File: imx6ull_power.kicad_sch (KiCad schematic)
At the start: 20 parts, among them U1 MX6UL-VM

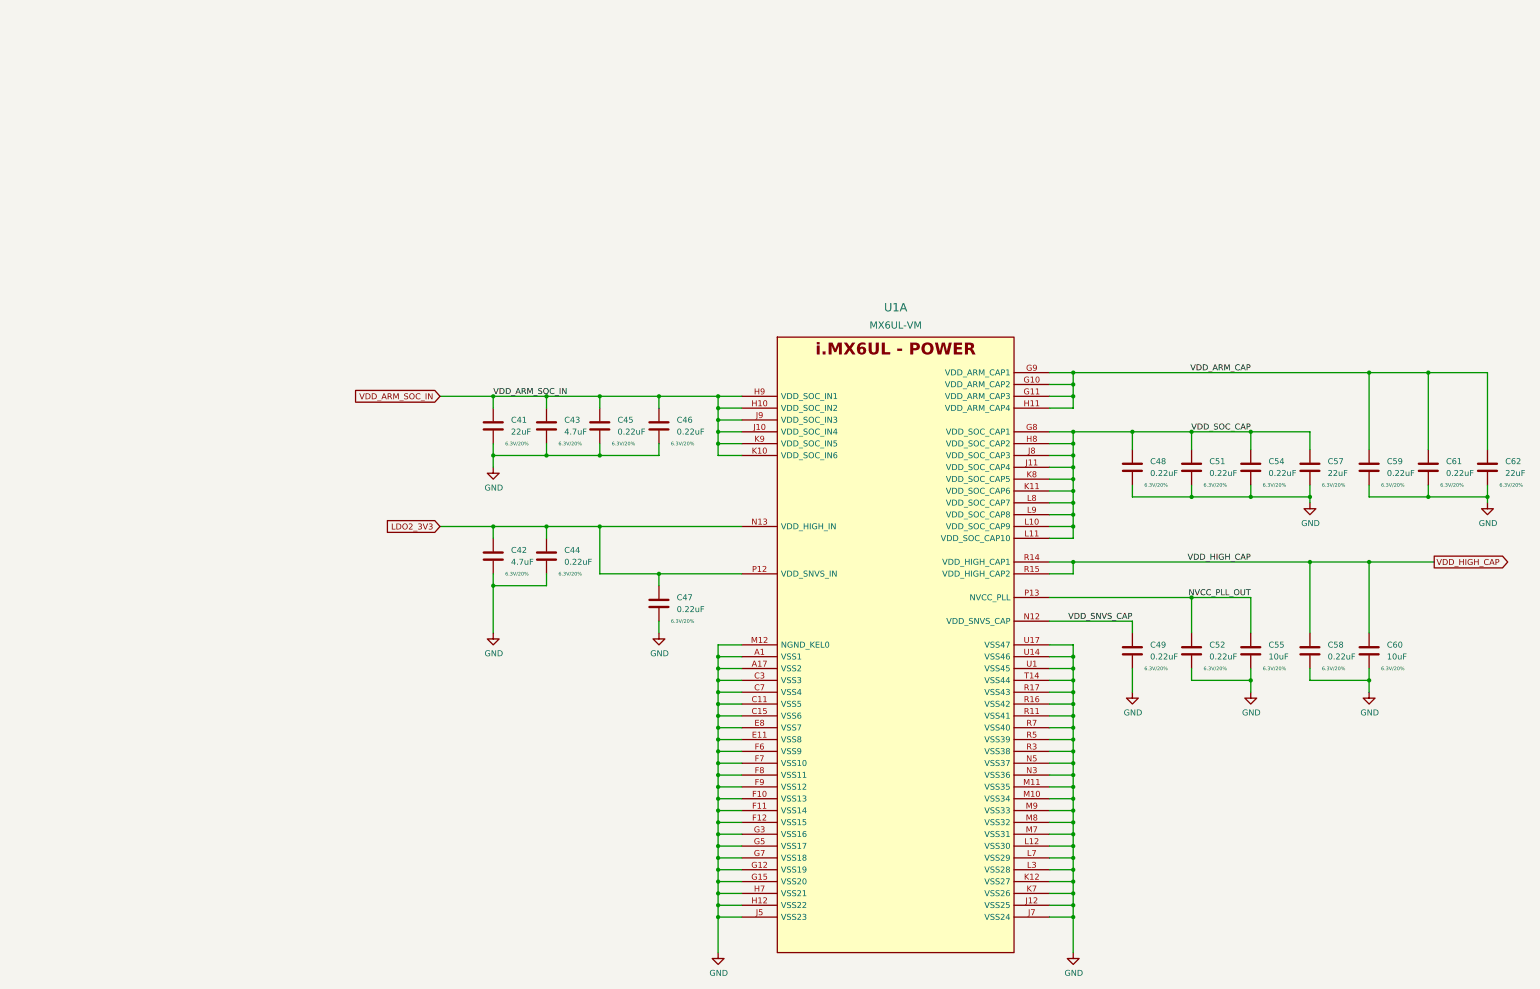
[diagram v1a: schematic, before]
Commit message: start moving to hierarchal labels, add emmc
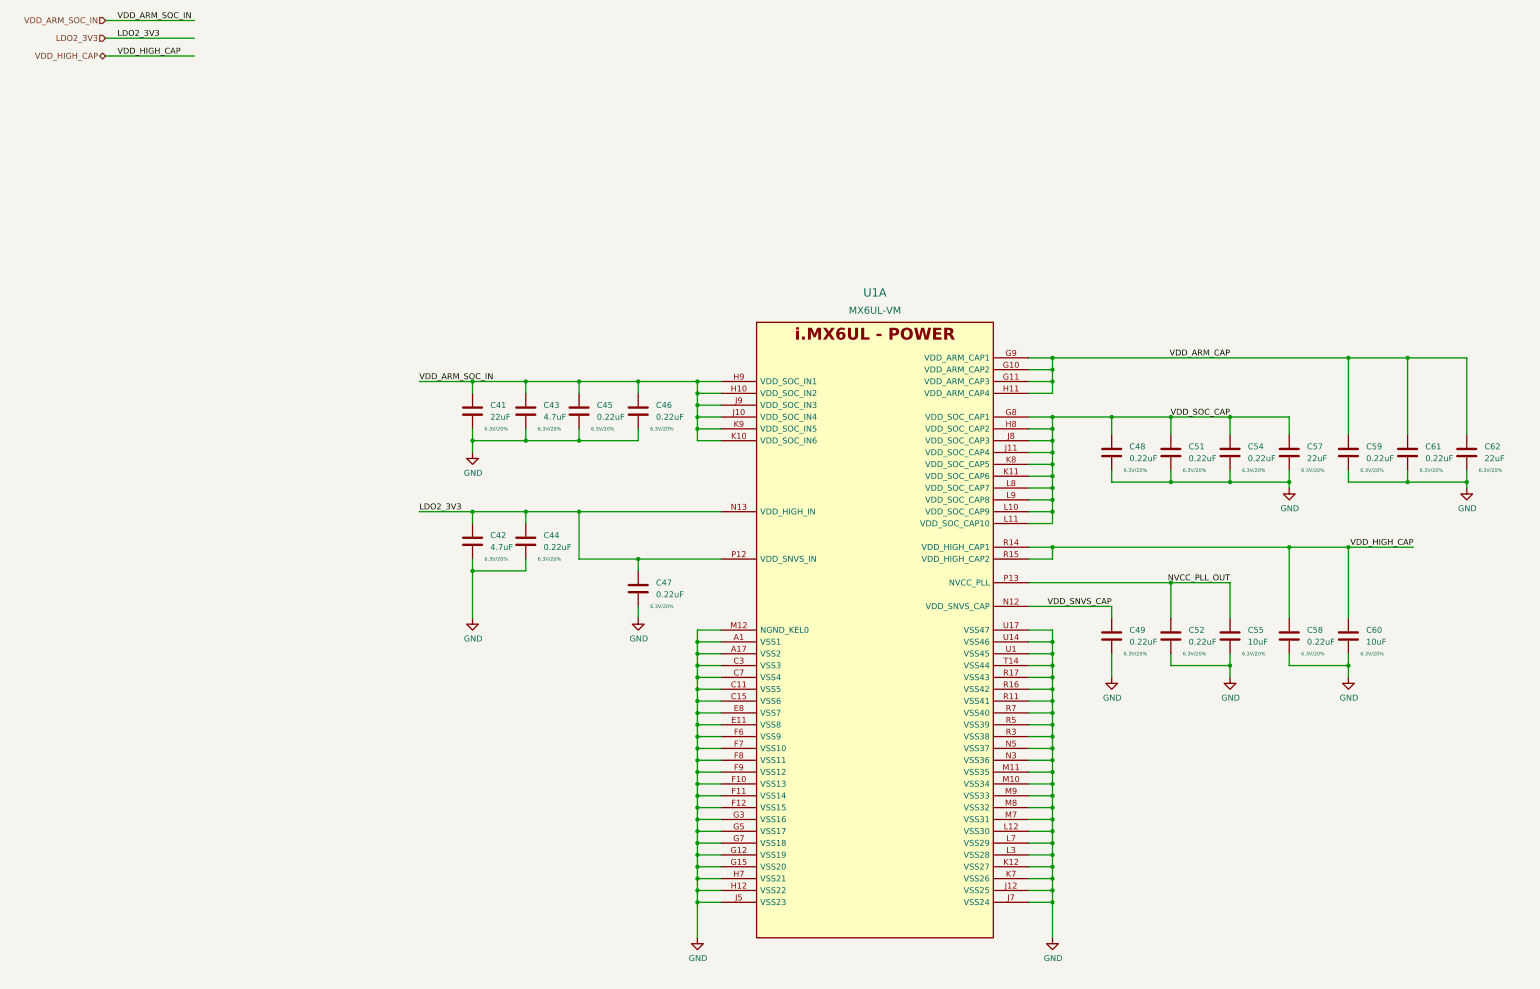
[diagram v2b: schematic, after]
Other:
- moved on the sheet: C41, C42, C43, C44, C45, C46, C47, C48, C49, C51, C52, C54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

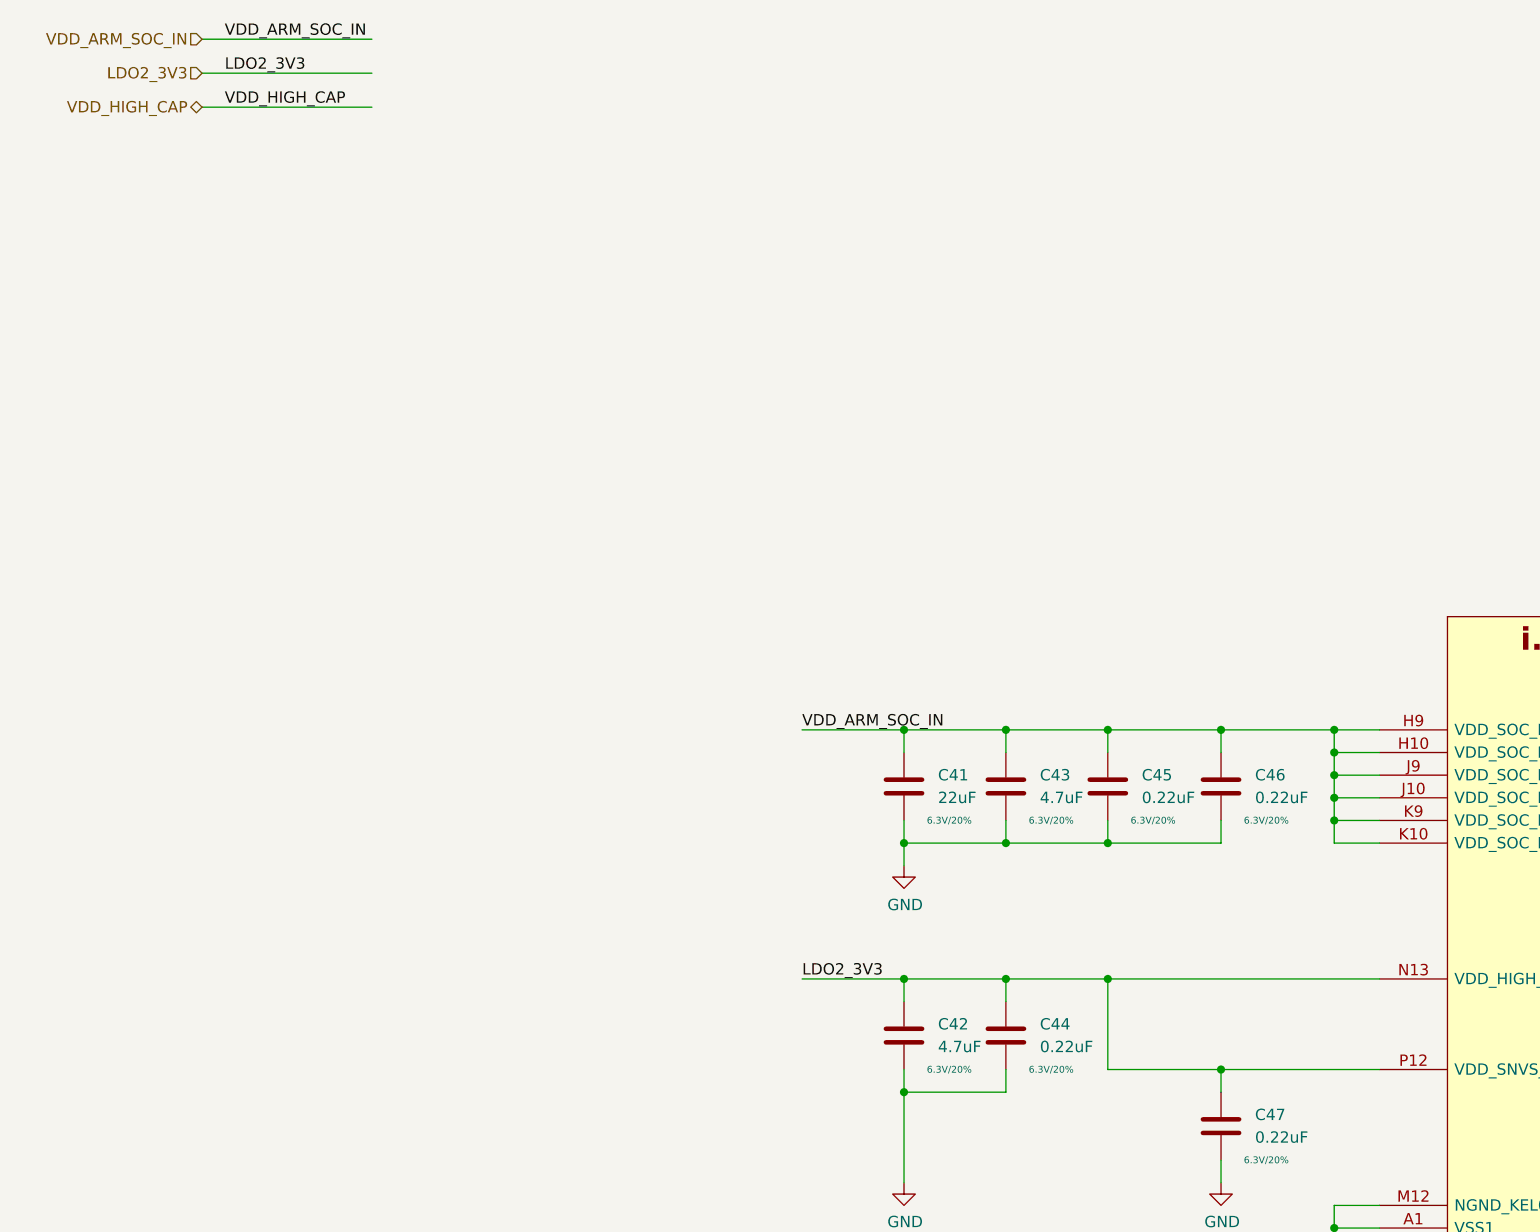
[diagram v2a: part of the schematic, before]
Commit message: move to hierarchal labels, work on power tree, add basic pcb layout
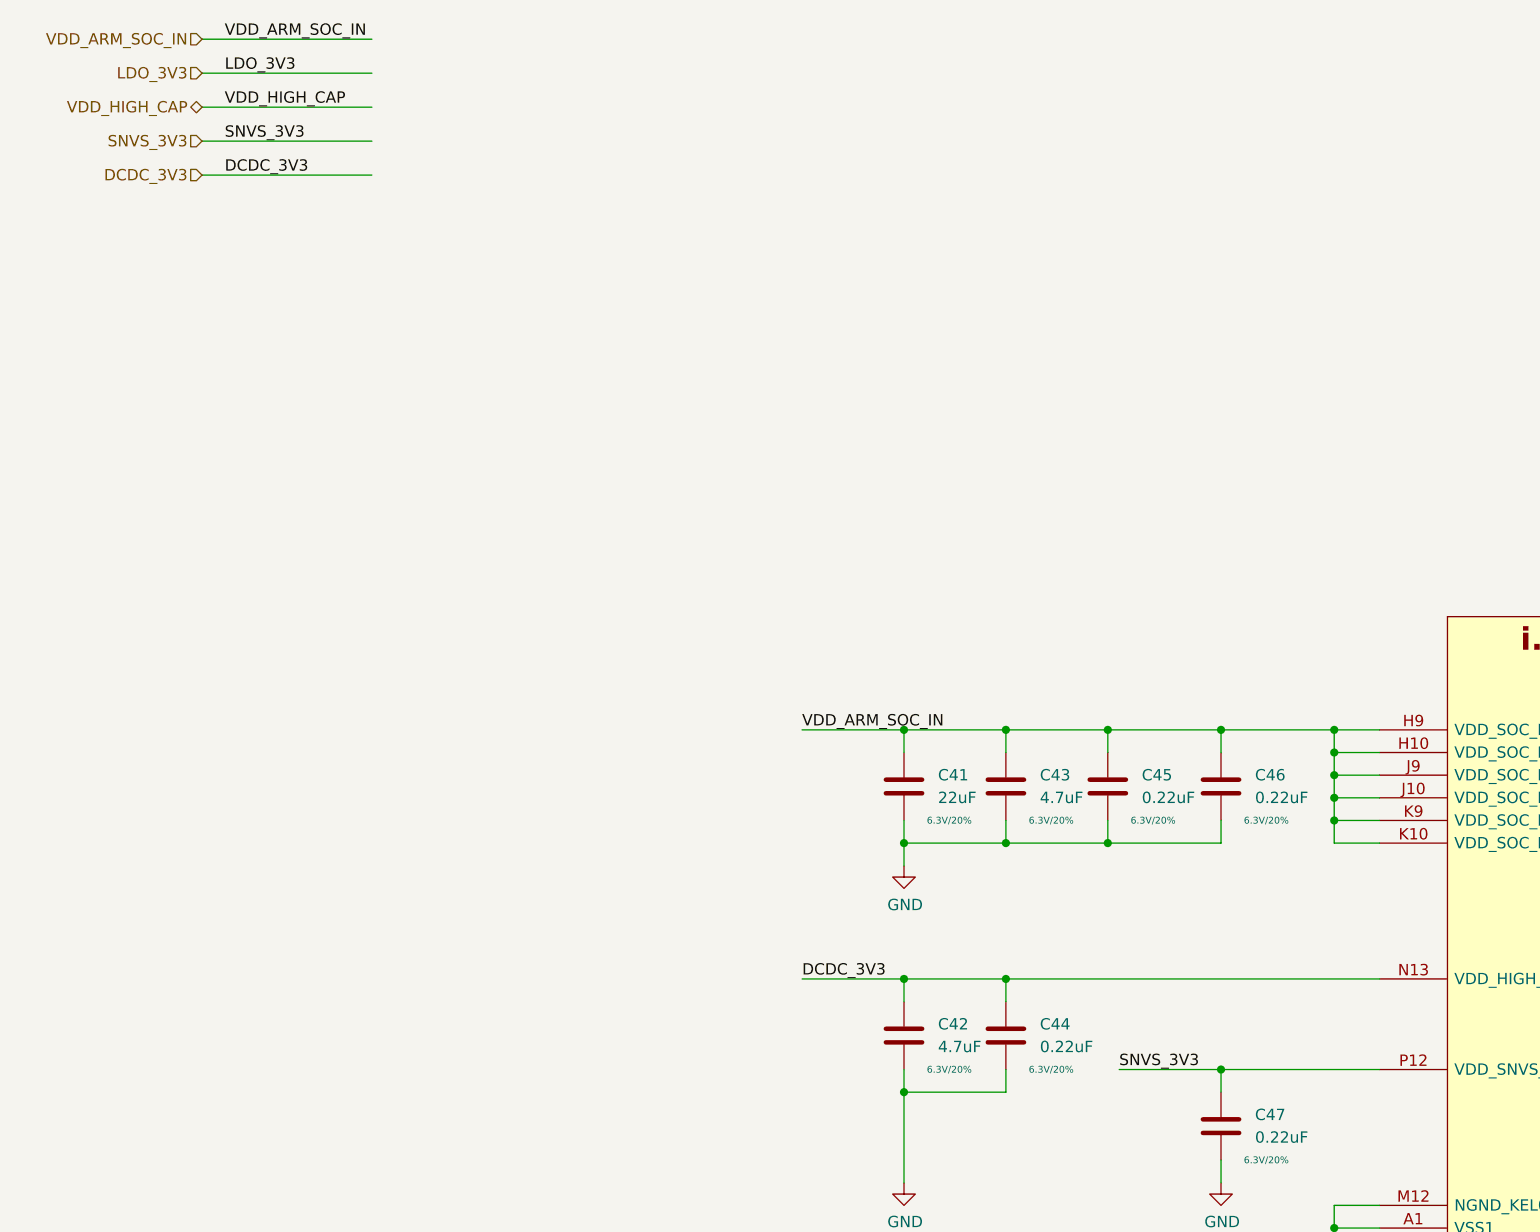
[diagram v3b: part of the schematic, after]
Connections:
- net LDO2_3V3 renamed DCDC_3V3
- net DCDC_3V3: no longer C47.1, U1.P12 (VDD_SNVS_IN)
- new net SNVS_3V3: C47.1, U1.P12 (VDD_SNVS_IN)
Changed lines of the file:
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@@
   (junction (at 237.49 175.26) (diameter 0) (color 0 0 0 0)
   )
+  (junction (at 148.59 137.16) (diameter 0) (color 0 0 0 0)
+  )
   (junction (at 237.49 119.38) (diameter 0) (color 0 0 0 0)
   )
@@
   (junction (at 113.03 111.76) (diameter 0) (color 0 0 0 0)
   )
-  (junction (at 148.59 137.16) (diameter 0) (color 0 0 0 0)
-  )
   (junction (at 237.49 200.66) (diameter 0) (color 0 0 0 0)
   )
@@
   (junction (at 161.29 172.72) (diameter 0) (color 0 0 0 0)
   )
-  (junction (at 135.89 127) (diameter 0) (color 0 0 0 0)
-  )
   (junction (at 237.49 172.72) (diameter 0) (color 0 0 0 0)
   )
@@
     (stroke (width 0) (type default) (color 0 0 0 0))
   )
+  (wire (pts (xy 34.29 33.02) (xy 53.34 33.02))
+    (stroke (width 0) (type default) (color 0 0 0 0))
+  )
   (wire (pts (xy 166.37 208.28) (xy 161.29 208.28))
     (stroke (width 0) (type default) (color 0 0 0 0))
@@
     (stroke (width 0) (type default) (color 0 0 0 0))
   )
-  (wire (pts (xy 135.89 137.16) (xy 148.59 137.16))
-    (stroke (width 0) (type default) (color 0 0 0 0))
-  )
   (wire (pts (xy 232.41 195.58) (xy 237.49 195.58))
     (stroke (width 0) (type default) (color 0 0 0 0))
@@
     (stroke (width 0) (type default) (color 0 0 0 0))
   )
+  (wire (pts (xy 34.29 36.83) (xy 53.34 36.83))
+    (stroke (width 0) (type default) (color 0 0 0 0))
+  )
   (wire (pts (xy 237.49 162.56) (xy 237.49 165.1))
     (stroke (width 0) (type default) (color 0 0 0 0))
@@
     (stroke (width 0) (type default) (color 0 0 0 0))
   )
-  (wire (pts (xy 124.46 127) (xy 135.89 127))
-    (stroke (width 0) (type default) (color 0 0 0 0))
-  )
   (wire (pts (xy 232.41 127) (xy 237.49 127))
     (stroke (width 0) (type default) (color 0 0 0 0))
@@
     (stroke (width 0) (type default) (color 0 0 0 0))
   )
+  (wire (pts (xy 137.16 137.16) (xy 148.59 137.16))
+    (stroke (width 0) (type default) (color 0 0 0 0))
+  )
   (wire (pts (xy 161.29 190.5) (xy 161.29 193.04))
     (stroke (width 0) (type default) (color 0 0 0 0))
@@
     (stroke (width 0) (type default) (color 0 0 0 0))
   )
-  (wire (pts (xy 135.89 127) (xy 166.37 127))
+  (wire (pts (xy 124.46 127) (xy 166.37 127))
     (stroke (width 0) (type default) (color 0 0 0 0))
   )
@@
   )
   (wire (pts (xy 313.69 118.11) (xy 313.69 120.65))
-    (stroke (width 0) (type default) (color 0 0 0 0))
-  )
-  (wire (pts (xy 135.89 137.16) (xy 135.89 127))
     (stroke (width 0) (type default) (color 0 0 0 0))
   )
@@
     (effects (font (size 1.27 1.27)) (justify right bottom))
   )
+  (label "SNVS_3V3" (at 137.16 137.16 0)
+    (effects (font (size 1.27 1.27)) (justify left bottom))
+  )
+  (label "DCDC_3V3" (at 36.83 36.83 0)
+    (effects (font (size 1.27 1.27)) (justify left bottom))
+  )
   (label "VDD_HIGH_CAP" (at 36.83 29.21 0)
     (effects (font (size 1.27 1.27)) (justify left bottom))
   )
+  (label "SNVS_3V3" (at 36.83 33.02 0)
+    (effects (font (size 1.27 1.27)) (justify left bottom))
+  )
   (label "NVCC_PLL_OUT" (at 275.59 142.24 180)
     (effects (font (size 1.27 1.27)) (justify right bottom))
   )
-  (label "LDO2_3V3" (at 36.83 25.4 0)
+  (label "LDO_3V3" (at 36.83 25.4 0)
     (effects (font (size 1.27 1.27)) (justify left bottom))
   )
@@
     (effects (font (size 1.27 1.27)) (justify left bottom))
   )
-  (label "LDO2_3V3" (at 101.6 127 0)
+  (label "DCDC_3V3" (at 101.6 127 0)
     (effects (font (size 1.27 1.27)) (justify left bottom))
   )
@@
     (effects (font (size 1.27 1.27)) (justify right))
   )
+  (hierarchical_label "SNVS_3V3" (shape input) (at 34.29 33.02 180)
+    (effects (font (size 1.27 1.27)) (justify right))
+  )
   (hierarchical_label "VDD_HIGH_CAP" (shape bidirectional) (at 34.29 29.21 180)
     (effects (font (size 1.27 1.27)) (justify right))
   )
-  (hierarchical_label "LDO2_3V3" (shape input) (at 34.29 25.4 180)
+  (hierarchical_label "DCDC_3V3" (shape input) (at 34.29 36.83 180)
     (effects (font (size 1.27 1.27)) (justify right))
   )
+  (hierarchical_label "LDO_3V3" (shape input) (at 34.29 25.4 180)
+    (effects (font (size 1.27 1.27)) (justify right))
+  )

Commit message: lots of routing, ddr length matching done
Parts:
- U1: footprint imx6ull-sbc:SOT1534-2 -> qsbc-zero:SOT1534-2; symbol imx6ull-sbc:MX6UL-VM -> qsbc-zero:MX6UL-VM
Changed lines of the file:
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@@
     (pin "2")
   )
-  (symbol (lib_id "imx6ull-sbc:MX6UL-VM") (at 199.39 86.36 0) (unit 1)
+  (symbol (lib_id "qsbc-zero:MX6UL-VM") (at 199.39 86.36 0) (unit 1)
     (in_bom yes) (on_board yes) (fields_autoplaced)
     (property "Reference" "U1" (id 0) (at 199.39 80.01 0)
@@
       (effects (font (size 1.524 1.524)))
     )
-    (property "Footprint" "imx6ull-sbc:SOT1534-2" (id 2) (at 212.344 115.824 0)
+    (property "Footprint" "qsbc-zero:SOT1534-2" (id 2) (at 212.344 115.824 0)
       (effects (font (size 1.524 1.524)) hide)
     )
